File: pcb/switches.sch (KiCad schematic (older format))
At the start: 58 parts

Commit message: Schematic version 1.0
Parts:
- removed JP?: Jumper_NO_Small, symbol Device:Jumper_NO_Small
- removed U?: 74LVC1G332, symbol 74xGxx:74LVC1G332
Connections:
- net labels removed: RST
- wire segments 145 -> 140
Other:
- note removed: "HARDWARE RESET\n"
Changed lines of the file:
@@
 $Descr A4 11693 8268
 encoding utf-8
-Sheet 3 3
+Sheet 2 3
 Title ""
 Date ""
@@
 	8900 5650 8900 5950
 $Comp
-L 74xGxx:74LVC1G332 U?
-U 1 1 61BF4492
-P 9500 3450
-F 0 "U?" H 9500 3764 50  0000 C CNN
-F 1 "74LVC1G332" H 9500 3673 50  0000 C CNN
-F 2 "" H 9500 3450 50  0001 C CNN
-F 3 "http://www.ti.com/lit/sg/scyt129e/scyt129e.pdf" H 9500 3450 50  0001 C CNN
-	1    9500 3450
-	1    0    0    -1
-$EndComp
-Text GLabel 9050 3350 0    50   Input ~ 0
-Button_1
-Text GLabel 9050 3450 0    50   Input ~ 0
-Button_5
-Text GLabel 9050 3550 0    50   Input ~ 0
-Button_9
-Wire Wire Line
-	9050 3350 9200 3350
-Wire Wire Line
-	9050 3450 9200 3450
-Wire Wire Line
-	9050 3550 9200 3550
-Text GLabel 10700 3450 2    50   Output ~ 0
-RST
-Wire Notes Line
-	8550 3750 11000 3750
-Wire Notes Line
-	11000 3750 11000 3000
-Wire Notes Line
-	11000 3000 8550 3000
-Wire Notes Line
-	8550 3000 8550 3750
-Text Notes 8550 2950 0    50   ~ 0
-HARDWARE RESET\n
-$Comp
 L power:GND #PWR?
 U 1 1 61C306D8
@@
 Wire Wire Line
 	2100 7000 2250 7000
-$Comp
-L Device:Jumper_NO_Small JP?
-U 1 1 61958962
-P 10250 3450
-F 0 "JP?" H 10250 3635 50  0000 C CNN
-F 1 "Jumper_NO_Small" H 10250 3544 50  0000 C CNN
-F 2 "" H 10250 3450 50  0001 C CNN
-F 3 "~" H 10250 3450 50  0001 C CNN
-	1    10250 3450
-	1    0    0    -1
-$EndComp
-Wire Wire Line
-	10350 3450 10700 3450
-Wire Wire Line
-	9800 3450 10150 3450
 $EndSCHEMATC

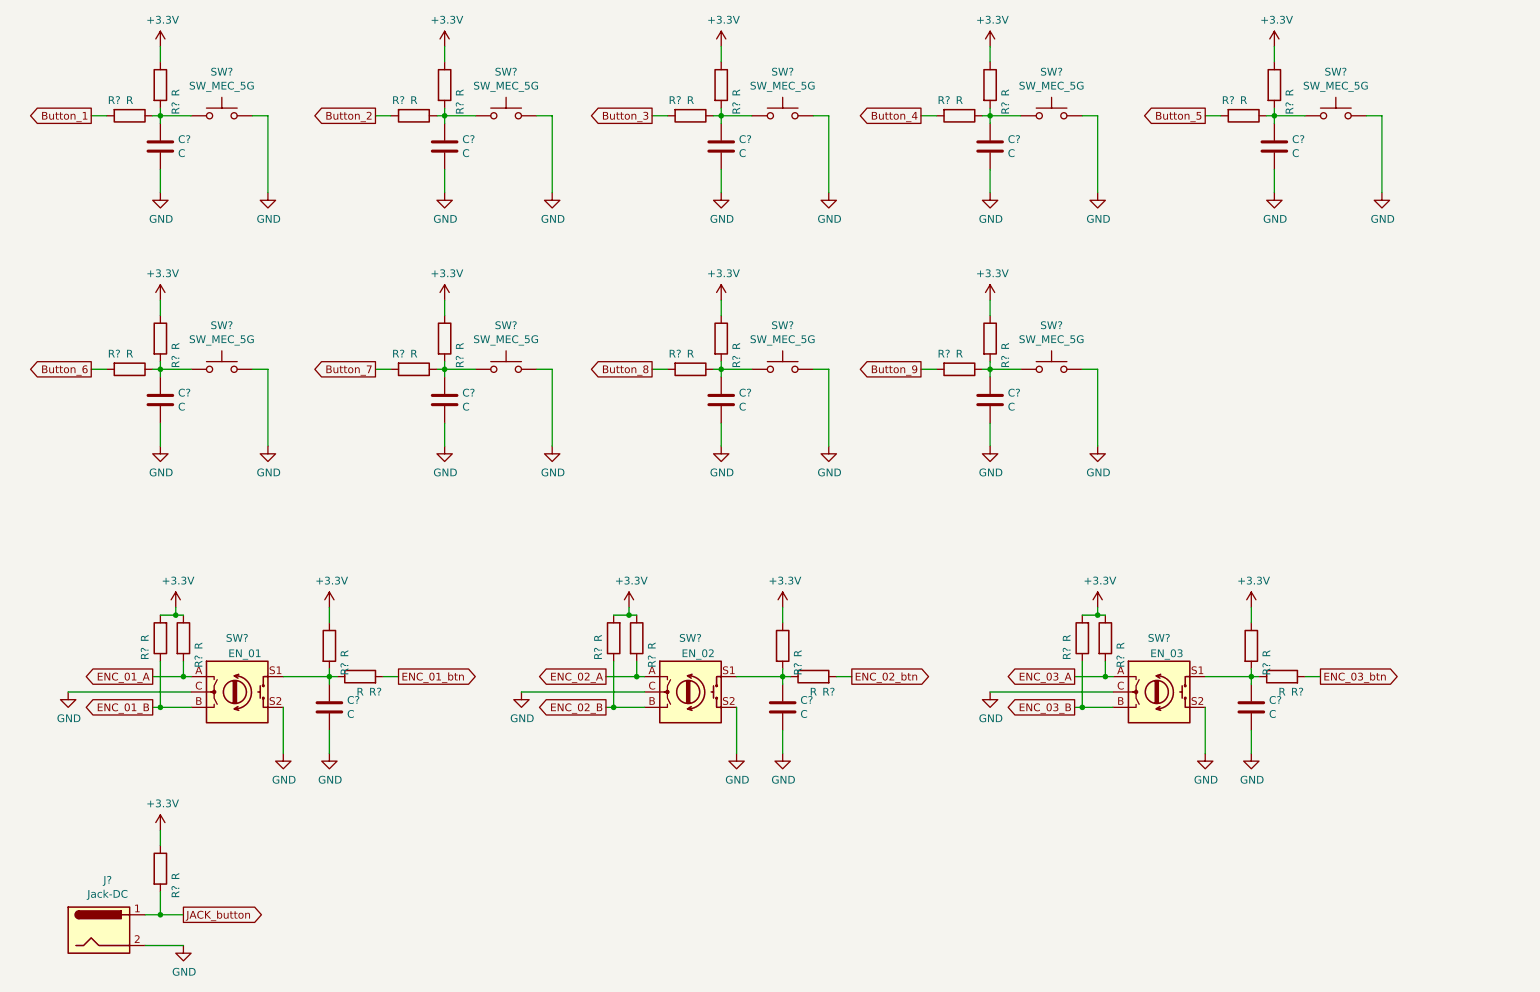
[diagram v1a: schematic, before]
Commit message: Added EEPROM memory & some footprints
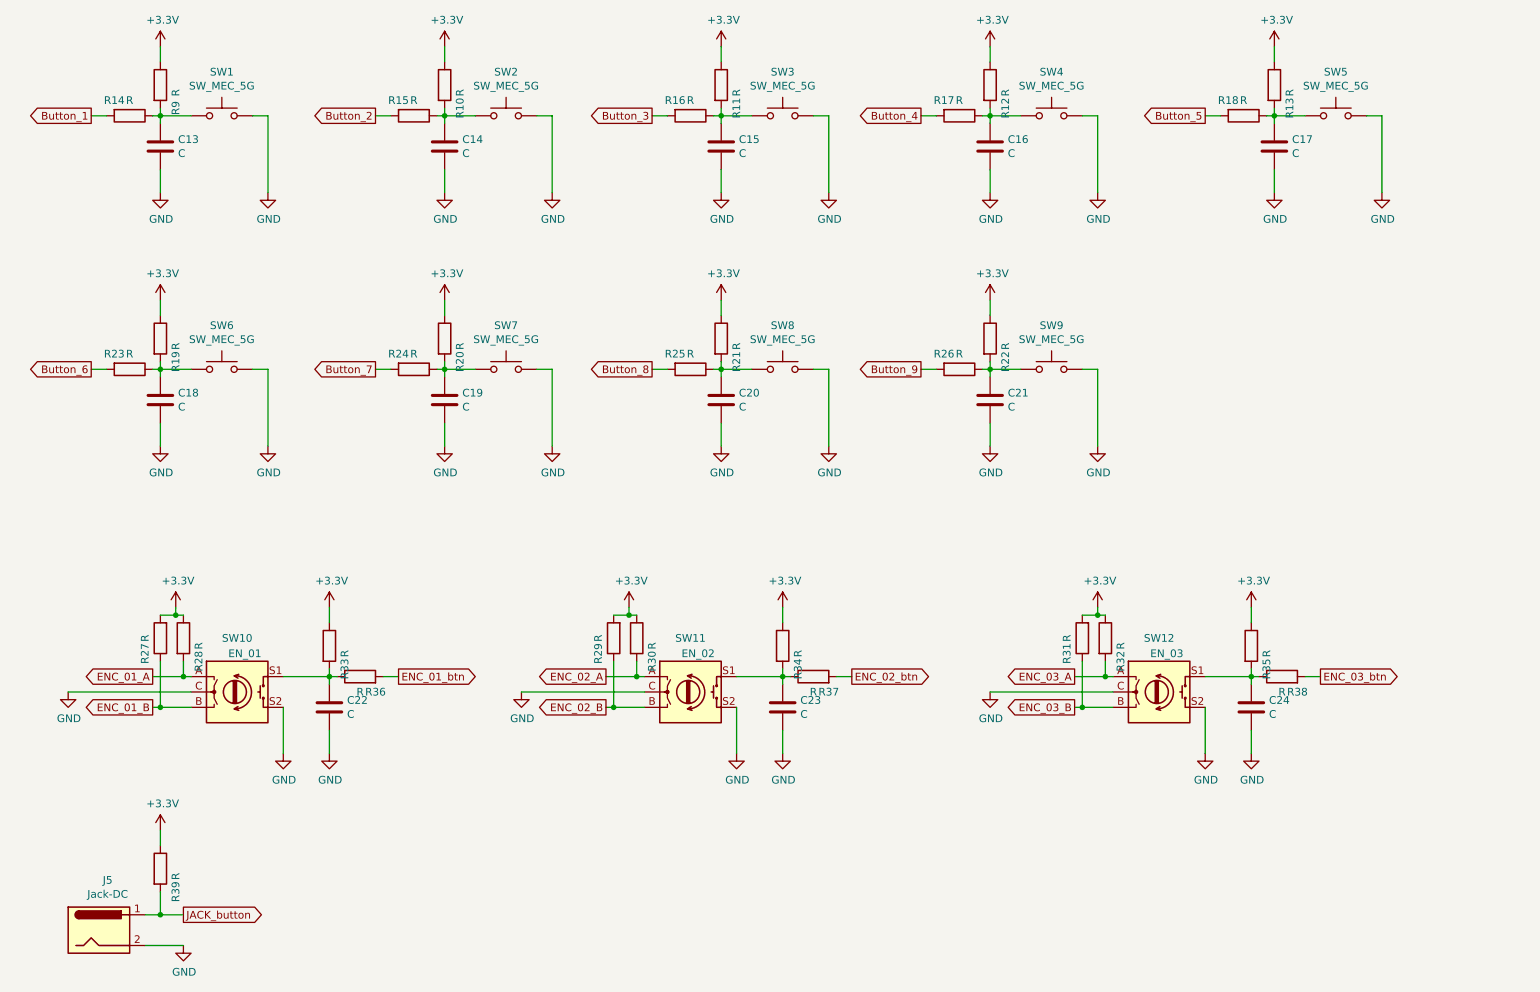
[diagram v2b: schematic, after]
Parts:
- SW10, SW11, SW12: renamed from SW?; footprint (none) -> Rotary_Encoder:RotaryEncoder_Alps_EC11E-Switch_Vertical_H20mm_CircularMountingHoles
- gave numbers to parts that had none: 53

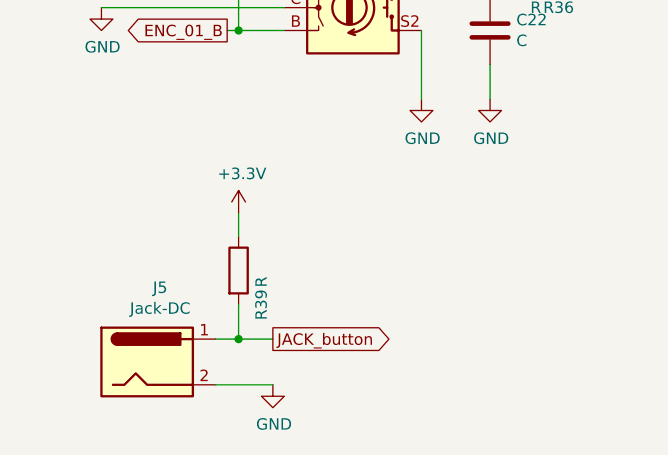
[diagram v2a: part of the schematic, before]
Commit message: Finish schematic and added footprints
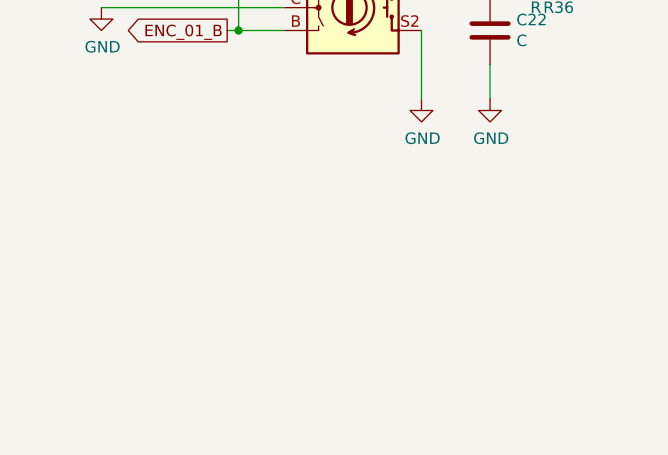
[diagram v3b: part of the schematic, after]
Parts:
- removed J5: Jack-DC, symbol Connector:Jack-DC
- removed R39: R, symbol Device:R
- C13, C14, C15, C16, C17, C18, C19, C20, C21, C22, C23, C24: footprint (none) -> Capacitor_SMD:C_0603_1608Metric
- R10, R11, R12, R13, R14, R15, R21, R22, R23, R24, R25, R26, R27, R28, R29, R30, R31, R32, R33, R34, R35, R36, R37, R38, R9: footprint (none) -> Resistor_SMD:R_0603_1608Metric
- R16, R17, R18, R19, R20: footprint (none) -> Resistor_SMD:R_0402_1005Metric_Pad0.72x0.64mm_HandSolder
- SW1, SW2, SW3, SW4, SW5, SW6, SW7, SW8, SW9: footprint (none) -> Button_Switch_Keyboard:SW_Cherry_MX_1.00u_PCB

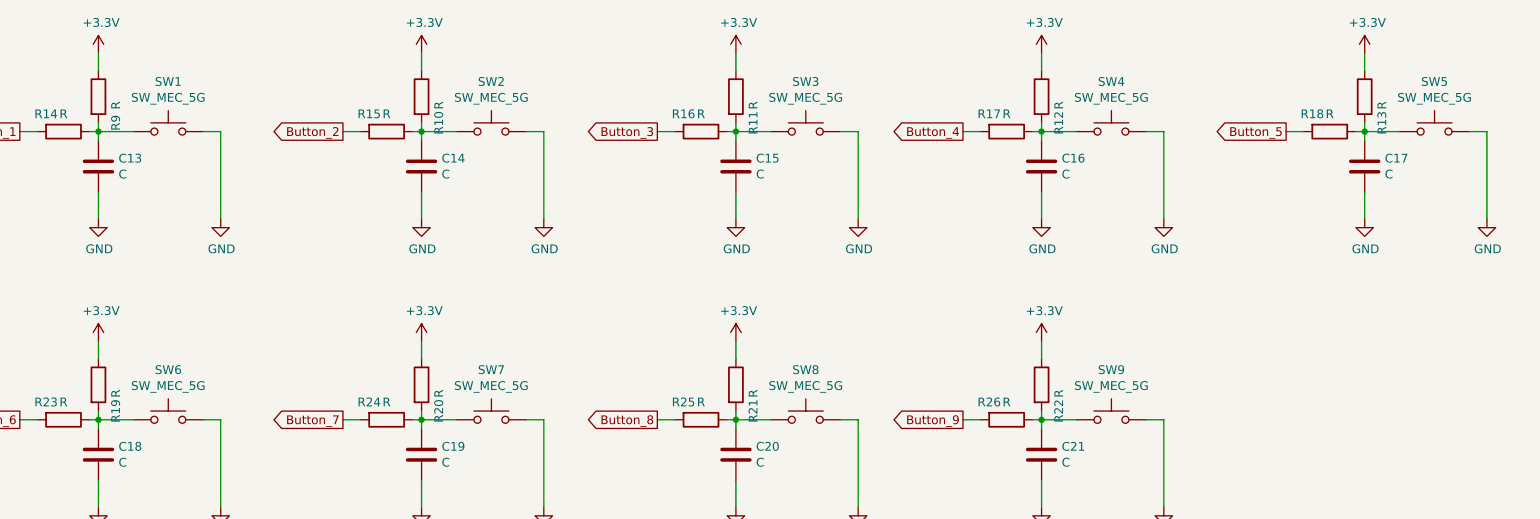
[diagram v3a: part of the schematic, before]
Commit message: Footprints update and some changes
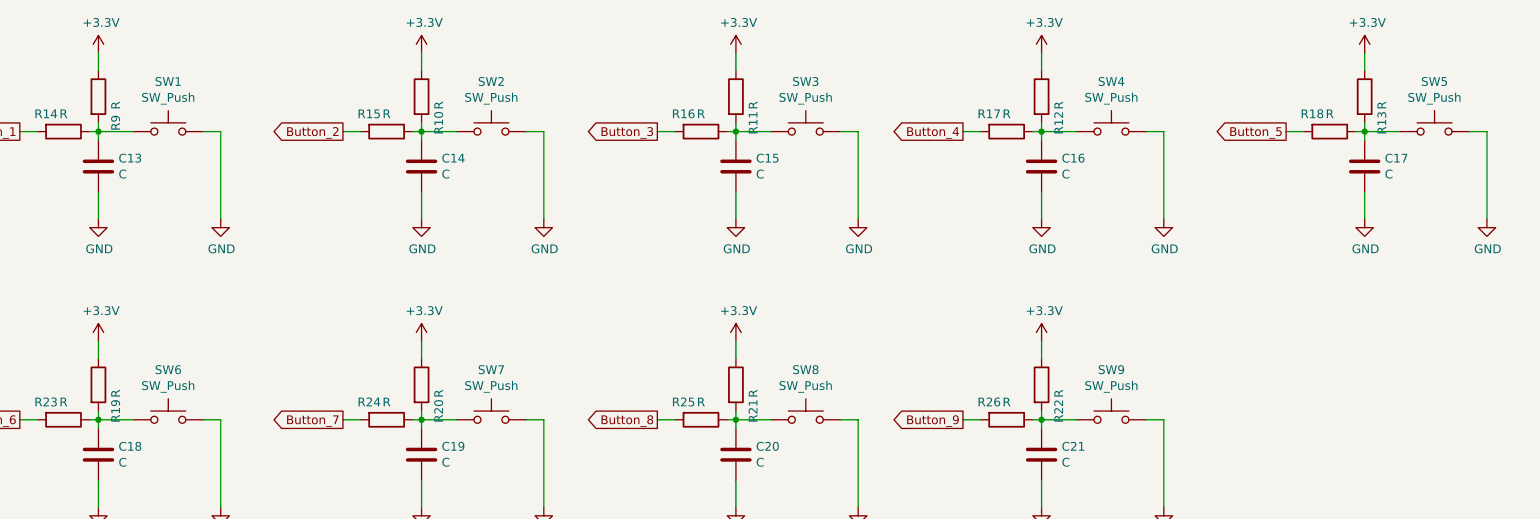
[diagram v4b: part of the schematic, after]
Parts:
- removed SW1, SW2, SW3, SW4, SW5, SW6, SW7, SW8, SW9: SW_MEC_5G, Button_Switch_Keyboard:SW_Cherry_MX_1.00u_PCB, symbol Switch:SW_MEC_5G
- added SW1, SW2, SW3, SW4, SW5, SW6, SW7, SW8, SW9: SW_Push, Button_Switch_Keyboard:SW_Cherry_MX_1.00u_PCB, symbol Switch:SW_Push
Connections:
- net GND: now also SW1.2, SW2.2, SW3.2, SW4.2, SW5.2, SW6.2, SW7.2, SW8.2, SW9.2
- net at C13.1, R14.1, R9.2: now also SW1.1
- net at C16.1, R12.2, R17.1: now also SW4.1
- net at C14.1, R10.2, R15.1: now also SW2.1
- net at C17.1, R13.2, R18.1: now also SW5.1
- net at C15.1, R11.2, R16.1: now also SW3.1
- net at C18.1, R19.2, R23.1: now also SW6.1
- net at C19.1, R20.2, R24.1: now also SW7.1
- net at C20.1, R21.2, R25.1: now also SW8.1
- net at C21.1, R22.2, R26.1: now also SW9.1
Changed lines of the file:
@@
 Wire Wire Line
 	1650 1800 1750 1800
-$Comp
-L Switch:SW_MEC_5G SW?
-U 1 1 61BCDF68
-P 2500 1800
-AR Path="/61BCDF68" Ref="SW?"  Part="1"
-AR Path="/61B99CE8/61BCDF68" Ref="SW1"  Part="1"
-F 0 "SW1" H 2500 2085 50  0000 C CNN
-F 1 "SW_MEC_5G" H 2500 1994 50  0000 C CNN
-F 2 "Button_Switch_Keyboard:SW_Cherry_MX_1.00u_PCB" H 2500 2000 50  0001 C CNN
-F 3 "http://www.apem.com/int/index.php?controller=attachment&id_attachment=488" H 2500 2000 50  0001 C CNN
-	1    2500 1800
-	1    0    0    -1
-$EndComp
 Wire Wire Line
 	2700 1800 2800 1800
@@
 Wire Wire Line
 	7050 1800 7150 1800
-$Comp
-L Switch:SW_MEC_5G SW?
-U 1 1 61BCDF9D
-P 7900 1800
-AR Path="/61BCDF9D" Ref="SW?"  Part="1"
-AR Path="/61B99CE8/61BCDF9D" Ref="SW4"  Part="1"
-F 0 "SW4" H 7900 2085 50  0000 C CNN
-F 1 "SW_MEC_5G" H 7900 1994 50  0000 C CNN
-F 2 "Button_Switch_Keyboard:SW_Cherry_MX_1.00u_PCB" H 7900 2000 50  0001 C CNN
-F 3 "http://www.apem.com/int/index.php?controller=attachment&id_attachment=488" H 7900 2000 50  0001 C CNN
-	1    7900 1800
-	1    0    0    -1
-$EndComp
 Wire Wire Line
 	8100 1800 8200 1800
@@
 Wire Wire Line
 	3500 1800 3600 1800
-$Comp
-L Switch:SW_MEC_5G SW?
-U 1 1 61BCDFD2
-P 4350 1800
-AR Path="/61BCDFD2" Ref="SW?"  Part="1"
-AR Path="/61B99CE8/61BCDFD2" Ref="SW2"  Part="1"
-F 0 "SW2" H 4350 2085 50  0000 C CNN
-F 1 "SW_MEC_5G" H 4350 1994 50  0000 C CNN
-F 2 "Button_Switch_Keyboard:SW_Cherry_MX_1.00u_PCB" H 4350 2000 50  0001 C CNN
-F 3 "http://www.apem.com/int/index.php?controller=attachment&id_attachment=488" H 4350 2000 50  0001 C CNN
-	1    4350 1800
-	1    0    0    -1
-$EndComp
 Wire Wire Line
 	4550 1800 4650 1800
@@
 Wire Wire Line
 	8900 1800 9000 1800
-$Comp
-L Switch:SW_MEC_5G SW?
-U 1 1 61BCE007
-P 9750 1800
-AR Path="/61BCE007" Ref="SW?"  Part="1"
-AR Path="/61B99CE8/61BCE007" Ref="SW5"  Part="1"
-F 0 "SW5" H 9750 2085 50  0000 C CNN
-F 1 "SW_MEC_5G" H 9750 1994 50  0000 C CNN
-F 2 "Button_Switch_Keyboard:SW_Cherry_MX_1.00u_PCB" H 9750 2000 50  0001 C CNN
-F 3 "http://www.apem.com/int/index.php?controller=attachment&id_attachment=488" H 9750 2000 50  0001 C CNN
-	1    9750 1800
-	1    0    0    -1
-$EndComp
 Wire Wire Line
 	9950 1800 10050 1800
@@
 Wire Wire Line
 	5300 1800 5400 1800
-$Comp
-L Switch:SW_MEC_5G SW?
-U 1 1 61BCE03C
-P 6150 1800
-AR Path="/61BCE03C" Ref="SW?"  Part="1"
-AR Path="/61B99CE8/61BCE03C" Ref="SW3"  Part="1"
-F 0 "SW3" H 6150 2085 50  0000 C CNN
-F 1 "SW_MEC_5G" H 6150 1994 50  0000 C CNN
-F 2 "Button_Switch_Keyboard:SW_Cherry_MX_1.00u_PCB" H 6150 2000 50  0001 C CNN
-F 3 "http://www.apem.com/int/index.php?controller=attachment&id_attachment=488" H 6150 2000 50  0001 C CNN
-	1    6150 1800
-	1    0    0    -1
-$EndComp
 Wire Wire Line
 	6350 1800 6450 1800
@@
 Wire Wire Line
 	1650 3450 1750 3450
-$Comp
-L Switch:SW_MEC_5G SW?
-U 1 1 61BCE071
-P 2500 3450
-AR Path="/61BCE071" Ref="SW?"  Part="1"
-AR Path="/61B99CE8/61BCE071" Ref="SW6"  Part="1"
-F 0 "SW6" H 2500 3735 50  0000 C CNN
-F 1 "SW_MEC_5G" H 2500 3644 50  0000 C CNN
-F 2 "Button_Switch_Keyboard:SW_Cherry_MX_1.00u_PCB" H 2500 3650 50  0001 C CNN
-F 3 "http://www.apem.com/int/index.php?controller=attachment&id_attachment=488" H 2500 3650 50  0001 C CNN
-	1    2500 3450
-	1    0    0    -1
-$EndComp
 Wire Wire Line
 	2700 3450 2800 3450
@@
 Wire Wire Line
 	3500 3450 3600 3450
-$Comp
-L Switch:SW_MEC_5G SW?
-U 1 1 61BCE0A6
-P 4350 3450
-AR Path="/61BCE0A6" Ref="SW?"  Part="1"
-AR Path="/61B99CE8/61BCE0A6" Ref="SW7"  Part="1"
-F 0 "SW7" H 4350 3735 50  0000 C CNN
-F 1 "SW_MEC_5G" H 4350 3644 50  0000 C CNN
-F 2 "Button_Switch_Keyboard:SW_Cherry_MX_1.00u_PCB" H 4350 3650 50  0001 C CNN
-F 3 "http://www.apem.com/int/index.php?controller=attachment&id_attachment=488" H 4350 3650 50  0001 C CNN
-	1    4350 3450
-	1    0    0    -1
-$EndComp
 Wire Wire Line
 	4550 3450 4650 3450
@@
 Wire Wire Line
 	5300 3450 5400 3450
-$Comp
-L Switch:SW_MEC_5G SW?
-U 1 1 61BCE0DB
-P 6150 3450
-AR Path="/61BCE0DB" Ref="SW?"  Part="1"
-AR Path="/61B99CE8/61BCE0DB" Ref="SW8"  Part="1"
-F 0 "SW8" H 6150 3735 50  0000 C CNN
-F 1 "SW_MEC_5G" H 6150 3644 50  0000 C CNN
-F 2 "Button_Switch_Keyboard:SW_Cherry_MX_1.00u_PCB" H 6150 3650 50  0001 C CNN
-F 3 "http://www.apem.com/int/index.php?controller=attachment&id_attachment=488" H 6150 3650 50  0001 C CNN
-	1    6150 3450
-	1    0    0    -1
-$EndComp
 Wire Wire Line
 	6350 3450 6450 3450
@@
 Wire Wire Line
 	7050 3450 7150 3450
-$Comp
-L Switch:SW_MEC_5G SW?
-U 1 1 61BCE110
-P 7900 3450
-AR Path="/61BCE110" Ref="SW?"  Part="1"
-AR Path="/61B99CE8/61BCE110" Ref="SW9"  Part="1"
-F 0 "SW9" H 7900 3735 50  0000 C CNN
-F 1 "SW_MEC_5G" H 7900 3644 50  0000 C CNN
-F 2 "Button_Switch_Keyboard:SW_Cherry_MX_1.00u_PCB" H 7900 3650 50  0001 C CNN
-F 3 "http://www.apem.com/int/index.php?controller=attachment&id_attachment=488" H 7900 3650 50  0001 C CNN
-	1    7900 3450
-	1    0    0    -1
-$EndComp
 Wire Wire Line
 	8100 3450 8200 3450
@@
 Wire Wire Line
 	8900 5650 8900 5950
+$Comp
+L Switch:SW_Push SW6
+U 1 1 61F907D9
+P 2500 3450
+F 0 "SW6" H 2500 3735 50  0000 C CNN
+F 1 "SW_Push" H 2500 3644 50  0000 C CNN
+F 2 "Button_Switch_Keyboard:SW_Cherry_MX_1.00u_PCB" H 2500 3650 50  0001 C CNN
+F 3 "~" H 2500 3650 50  0001 C CNN
+	1    2500 3450
+	1    0    0    -1
+$EndComp
+$Comp
+L Switch:SW_Push SW1
+U 1 1 61FBF846
+P 2500 1800
+F 0 "SW1" H 2500 2085 50  0000 C CNN
+F 1 "SW_Push" H 2500 1994 50  0000 C CNN
+F 2 "Button_Switch_Keyboard:SW_Cherry_MX_1.00u_PCB" H 2500 2000 50  0001 C CNN
+F 3 "~" H 2500 2000 50  0001 C CNN
+	1    2500 1800
+	1    0    0    -1
+$EndComp
+$Comp
+L Switch:SW_Push SW2
+U 1 1 61FC48AC
+P 4350 1800
+F 0 "SW2" H 4350 2085 50  0000 C CNN
+F 1 "SW_Push" H 4350 1994 50  0000 C CNN
+F 2 "Button_Switch_Keyboard:SW_Cherry_MX_1.00u_PCB" H 4350 2000 50  0001 C CNN
+F 3 "~" H 4350 2000 50  0001 C CNN
+	1    4350 1800
+	1    0    0    -1
+$EndComp
+$Comp
+L Switch:SW_Push SW4
+U 1 1 61FC96E0
+P 7900 1800
+F 0 "SW4" H 7900 2085 50  0000 C CNN
+F 1 "SW_Push" H 7900 1994 50  0000 C CNN
+F 2 "Button_Switch_Keyboard:SW_Cherry_MX_1.00u_PCB" H 7900 2000 50  0001 C CNN
+F 3 "~" H 7900 2000 50  0001 C CNN
+	1    7900 1800
+	1    0    0    -1
+$EndComp
+$Comp
+L Switch:SW_Push SW7
+U 1 1 61FCE3A3
+P 4350 3450
+F 0 "SW7" H 4350 3735 50  0000 C CNN
+F 1 "SW_Push" H 4350 3644 50  0000 C CNN
+F 2 "Button_Switch_Keyboard:SW_Cherry_MX_1.00u_PCB" H 4350 3650 50  0001 C CNN
+F 3 "~" H 4350 3650 50  0001 C CNN
+	1    4350 3450
+	1    0    0    -1
+$EndComp
+$Comp
+L Switch:SW_Push SW9
+U 1 1 61FD3221
+P 7900 3450
+F 0 "SW9" H 7900 3735 50  0000 C CNN
+F 1 "SW_Push" H 7900 3644 50  0000 C CNN
+F 2 "Button_Switch_Keyboard:SW_Cherry_MX_1.00u_PCB" H 7900 3650 50  0001 C CNN
+F 3 "~" H 7900 3650 50  0001 C CNN
+	1    7900 3450
+	1    0    0    -1
+$EndComp
+$Comp
+L Switch:SW_Push SW3
+U 1 1 61FD80C0
+P 6150 1800
+F 0 "SW3" H 6150 2085 50  0000 C CNN
+F 1 "SW_Push" H 6150 1994 50  0000 C CNN
+F 2 "Button_Switch_Keyboard:SW_Cherry_MX_1.00u_PCB" H 6150 2000 50  0001 C CNN
+F 3 "~" H 6150 2000 50  0001 C CNN
+	1    6150 1800
+	1    0    0    -1
+$EndComp
+$Comp
+L Switch:SW_Push SW5
+U 1 1 61FDCDEB
+P 9750 1800
+F 0 "SW5" H 9750 2085 50  0000 C CNN
+F 1 "SW_Push" H 9750 1994 50  0000 C CNN
+F 2 "Button_Switch_Keyboard:SW_Cherry_MX_1.00u_PCB" H 9750 2000 50  0001 C CNN
+F 3 "~" H 9750 2000 50  0001 C CNN
+	1    9750 1800
+	1    0    0    -1
+$EndComp
+$Comp
+L Switch:SW_Push SW8
+U 1 1 61FE1CC4
+P 6150 3450
+F 0 "SW8" H 6150 3735 50  0000 C CNN
+F 1 "SW_Push" H 6150 3644 50  0000 C CNN
+F 2 "Button_Switch_Keyboard:SW_Cherry_MX_1.00u_PCB" H 6150 3650 50  0001 C CNN
+F 3 "~" H 6150 3650 50  0001 C CNN
+	1    6150 3450
+	1    0    0    -1
+$EndComp
 $EndSCHEMATC
